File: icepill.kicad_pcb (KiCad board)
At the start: 2 copper layers, 87.6 x 45.7 mm, 32 parts, among them IC1 iCE40UP5K-SG48, IC2 AZ1117H-1.2, J1 PMOD_1, J2 PMOD_2, J3 PMOD_3, J4 PMOD_4, J5 PMOD_5, J6 PMOD_6, J7 PMOD_7, J8 FPGA_A, J9 FPGA_B, U1 BlackPill, X1 M3_MOUNT, X2 M3_MOUNT, X3 M3_MOUNT, X4 M3_MOUNT

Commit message: Address first revision feedback.
* MCO from STM32 now routes to GB3 (pin 20), a global input.
* Consequently F_CLK is now present at PMOD2.2.
* PC14 and PC15 no longer connected as they have an LSE on the Black Pill.
* F_IRQ moved to PMOD1.4.
* 0R resistors for selecting IRQ and CLK presence at PMODs changed to
  allow either STM32 or iCE40 to drive the PMOD pin, while the iCE40
  remains always connected to the other STM32 pin providing IRQ/CLK.
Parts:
- added R7: DNF, icepill:0603, F.Cu at (64.5, 87.4)
- added R8: DNF, icepill:0603, F.Cu at (96.8, 85.9)
- moved R2 23.4 mm to (96.8, 87.6), turned to 0 degrees
- moved R3 5.24 mm to (64.5, 85.6), turned to 180 degrees
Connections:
- IC1 pad 20: /P2_2 -> /F_CLK
- IC1 pad 9: /P1_4 -> /F_~IRQ
- R2 pad 2: /P1_4 -> /P2_2
- R3 pad 2: /P1_3 -> /P1_4
- U1 pad 12: /P2_2 -> Net-(R8-Pad2)
- U1 pad 23: /P4_4 -> Net-(U1-Pad23)
- U1 pad 24: /P4_3 -> Net-(U1-Pad24)
- U1 pad 6: /P1_4 -> Net-(R7-Pad2)
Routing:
- net /F_CLK: track 10.7 -> 37.0 mm, vias 0 -> 3
- net Net-(R7-Pad2): track 0.00 -> 23.1 mm
- net /F_~IRQ: track 35.9 -> 56.3 mm
- net /P1_4: track 29.1 -> 13.9 mm
- net /P2_2: track 18.5 -> 7.38 mm
- net /P1_3: track 31.6 -> 22.9 mm, vias 1 -> 0
- net GND: track 19.5 -> 26.5 mm, vias 11 -> 15
- net Net-(R8-Pad2): track 0.00 -> 4.80 mm
- net 1v2: track 69.2 -> 71.8 mm
- net /P1_1: track 20.4 -> 22.2 mm
- net /P4_4: track 33.2 -> 34.4 mm
- net /P4_3: track 32.7 -> 33.9 mm
- net /P2_3: track 16.9 -> 17.7 mm
- net 3v3: track 295.7 -> 295.0 mm
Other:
- board text added: "3V 0V 9 10 11 12"
- board text added: "R3: P1.4⇿~IRQ~ (9) R7: P1.4⇿PA9"
- board text added: "R8: P2.2⇿PB4 R2: P2.2⇿MCO (20)"
- board text removed: "9 10 11 12"
- board text removed: "R2: 9⇿MCO"
- board text removed: "R3: 10⇿IRQ"

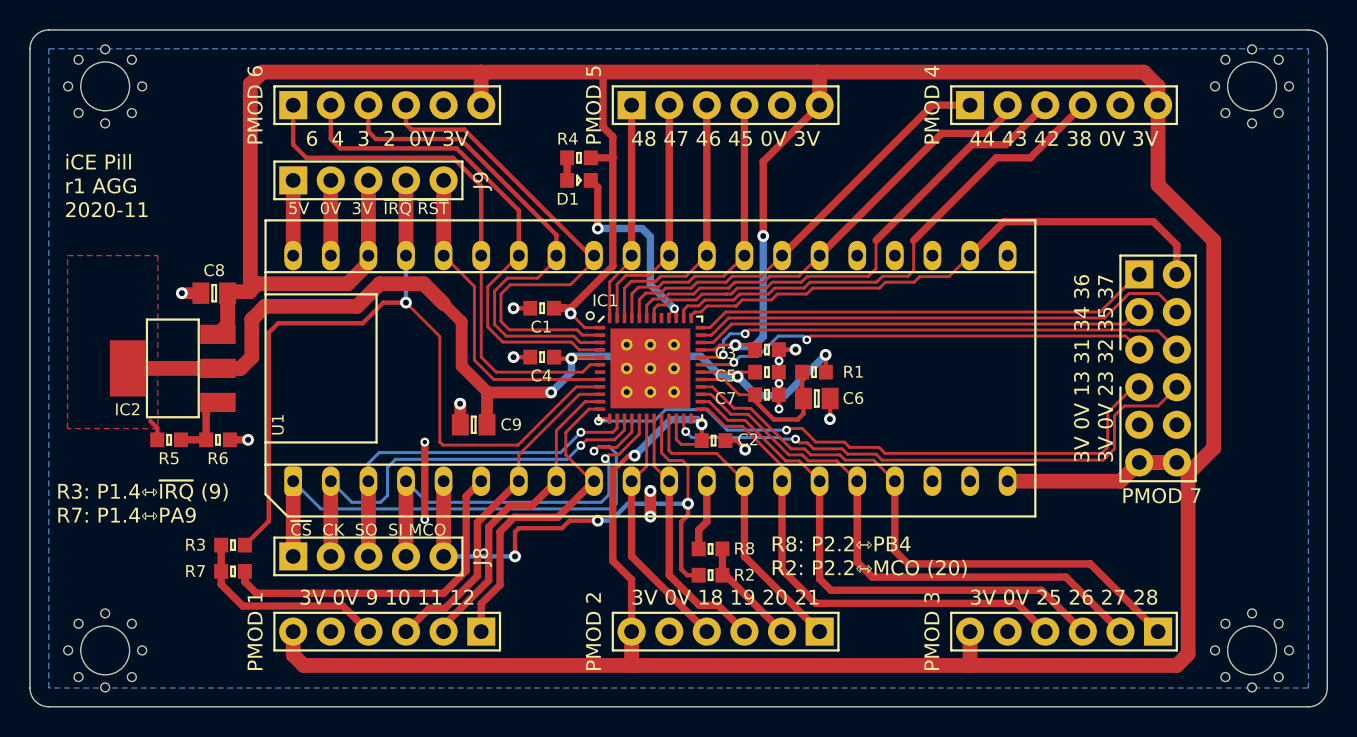
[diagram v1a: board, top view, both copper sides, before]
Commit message: Add pinout table to README, update render.
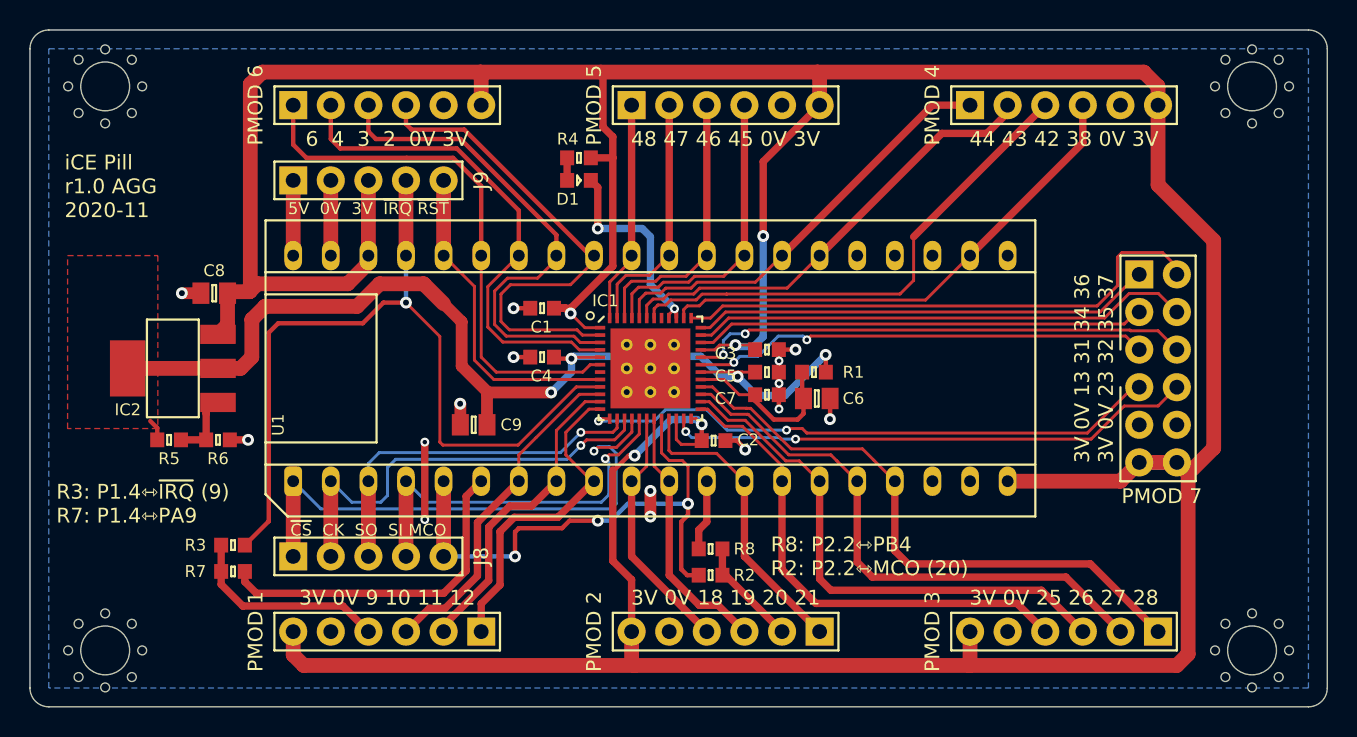
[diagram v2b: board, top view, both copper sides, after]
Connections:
- U1 pad 22: /P7_7 -> /P4_4
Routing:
- net /P7_4: track 42.2 -> 39.7 mm
- net /P7_10: track 38.2 -> 35.8 mm
- net /P7_7: track 38.2 -> 36.7 mm
- net /P4_3: track 33.9 -> 34.5 mm
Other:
- board text added: "iCE Pill r1.0 AGG 2020-11"
- board text removed: "iCE Pill r1 AGG 2020-11"

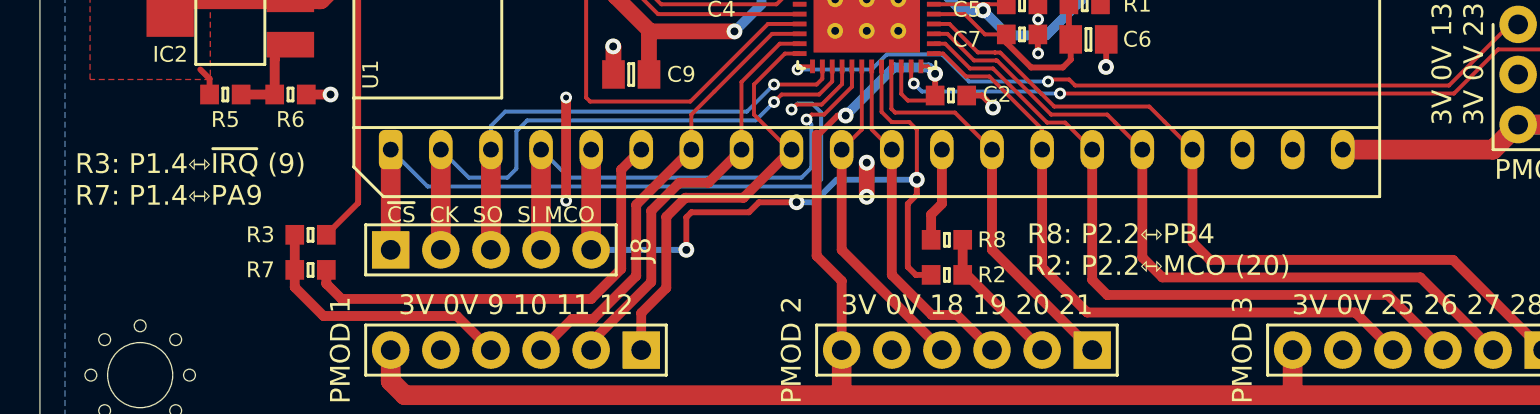
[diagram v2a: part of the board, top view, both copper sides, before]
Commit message: Update silk for R2/3/7/8
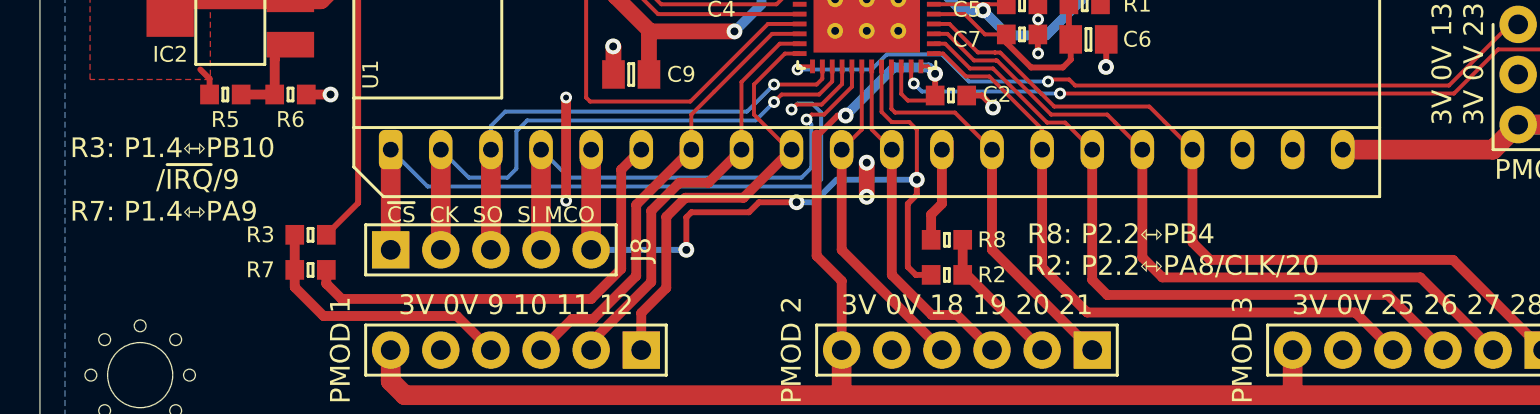
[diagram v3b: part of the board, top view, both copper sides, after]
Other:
- board text added: "R3: P1.4⇿PB10 /~IRQ~/9 R7: P1.4⇿PA9"
- board text added: "R8: P2.2⇿PB4 R2: P2.2⇿PA8/CLK/20"
- board text removed: "R3: P1.4⇿~IRQ~ (9) R7: P1.4⇿PA9"
- board text removed: "R8: P2.2⇿PB4 R2: P2.2⇿MCO (20)"
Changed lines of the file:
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@@
     )
   )
-  (gr_text "R8: P2.2⇿PB4\nR2: P2.2⇿MCO (20)" (at 100.838 86.36) (layer F.SilkS)
+  (gr_text "R8: P2.2⇿PB4\nR2: P2.2⇿PA8/CLK/20" (at 100.838 86.36) (layer F.SilkS)
     (effects (font (size 1 1) (thickness 0.15)) (justify left))
   )
-  (gr_text "R3: P1.4⇿~IRQ~ (9)\nR7: P1.4⇿PA9" (at 52.578 82.804) (layer F.SilkS)
+  (gr_text "R3: P1.4⇿PB10\n          /~IRQ~/9\nR7: P1.4⇿PA9" (at 52.324 82.804) (layer F.SilkS)
     (effects (font (size 1 1) (thickness 0.15)) (justify left))
   )
